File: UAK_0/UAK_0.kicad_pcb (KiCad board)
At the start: 2 copper layers, 100 x 90 mm, 79 parts, among them K1 Кнопка_FSMSM, K2 Кнопка_FSMSM, X1 Крепежное_отверстие_М3, X2 Крепежное_отверстие_М3, X3 Крепежное_отверстие_М3, X4 Крепежное_отверстие_М3, X5 Крепежное_отверстие_d2, X6 Крепежное_отверстие_d2, X7 Крепежное_отверстие_d2

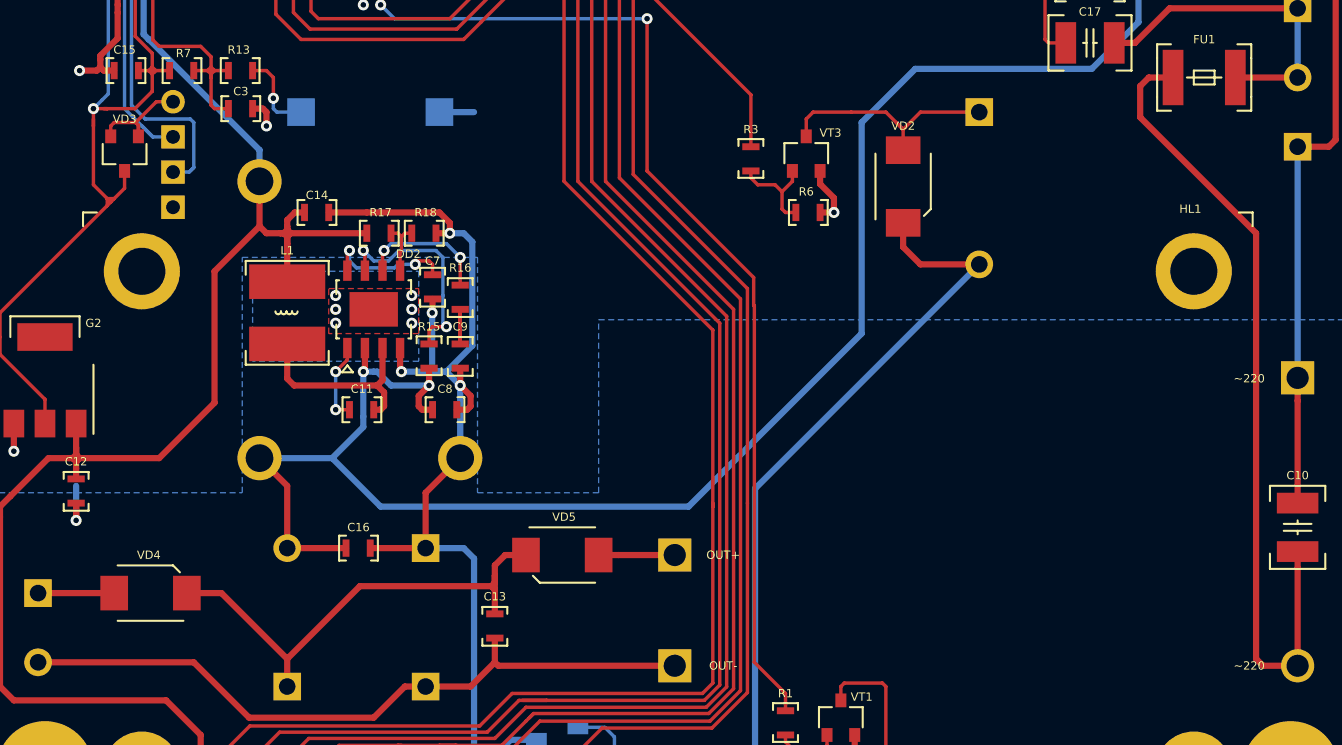
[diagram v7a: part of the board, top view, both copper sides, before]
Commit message: UAK.1A.M9
исправлено межоснвое растояние крепежки экрана, заменен диод закольцовки зумера на сопротивление 4,7 кОм
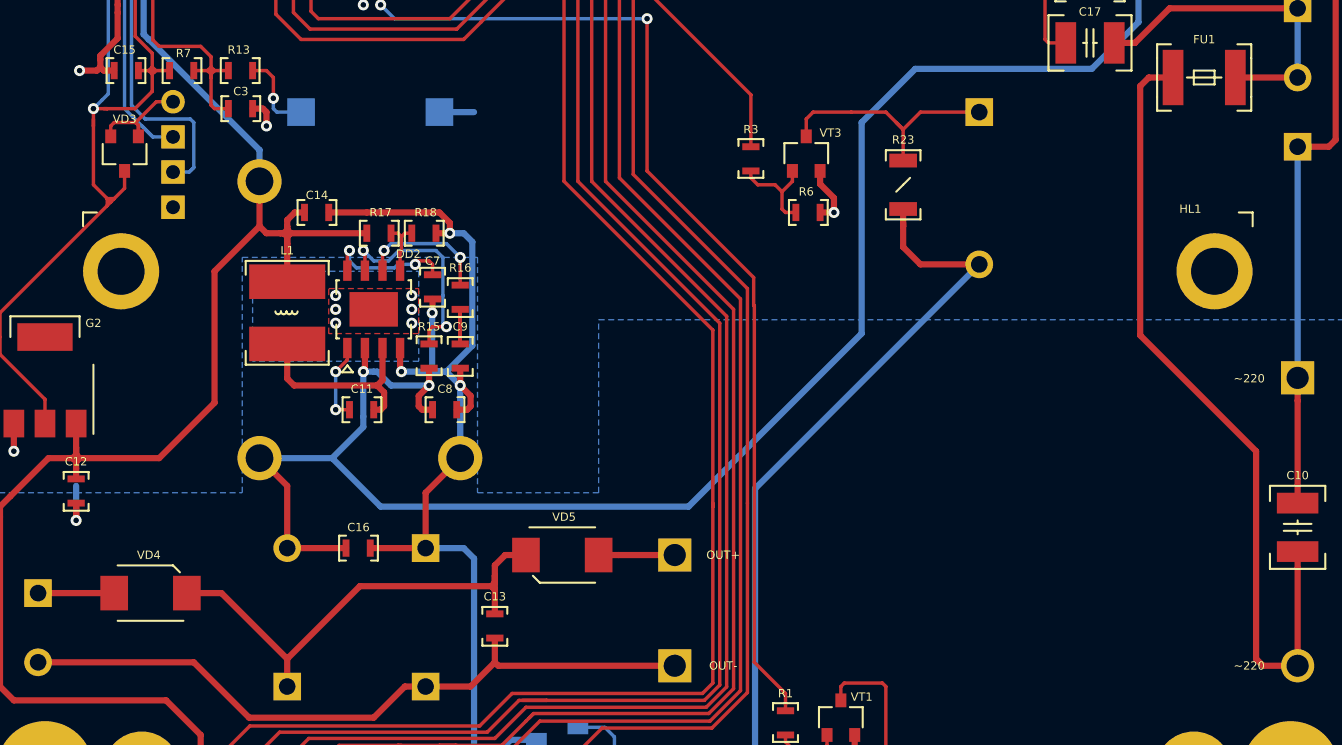
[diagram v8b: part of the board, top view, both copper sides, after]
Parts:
- removed VD2: Диод_шоттки_SK16, N_VD_HL:Диод_SMB
- added R23: Резистор_0,25Вт, N_RLC:Резистор_SMD_1206-0,25_Вт, F.Cu at (142.0, 94.5)
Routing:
- net /5V: track 305.4 -> 306.7 mm
- net Net-(HA1-Pad2): track 17.2 -> 17.9 mm
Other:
- board text added: "UAK.1A.M9"
- board text removed: "UAK.0C.M9"
